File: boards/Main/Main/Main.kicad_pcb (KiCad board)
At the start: 2 copper layers, 32 parts, among them J1 CAN_H, J10 Status_Light, J11 J00-0045NL, J12 IMU, J2 GND, J3 TX/RX, J4 5V, J5 Digital I/O, J6 CAN_Board, J7 CAN_L, J8 CAN H/L, J9 24V, K1 G5LE-1, K2 G5LE-1, K3 G5LE-1, K4 G5LE-1, Q1 2N3904, Q2 2N3904, Q3 2N3904, U1 Teensy4.1, U2 BNO055

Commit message: Updated Main PCB
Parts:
- removed 0.1uF1: C, Capacitor_THT:CP_Axial_L10.0mm_D4.5mm_P15.00mm_Horizontal
- removed CB1: Break1, Connector_PinHeader_2.54mm:PinHeader_1x01_P2.54mm_Vertical
- removed CB2: Break2, Connector_PinHeader_2.54mm:PinHeader_1x02_P2.54mm_Horizontal
- removed J1: CAN_H, Connector_PinHeader_2.54mm:PinHeader_1x01_P2.54mm_Vertical
- removed J10: Status_Light, Connector_PinHeader_2.54mm:PinHeader_1x04_P2.54mm_Vertical
- removed J11: J00-0045NL, teensy.pretty-master:PULSE_J00-0045NL
- removed J12: IMU, Connector_PinHeader_2.54mm:PinHeader_1x03_P2.54mm_Vertical
- removed J2: GND, Connector_PinHeader_2.54mm:PinHeader_1x04_P2.54mm_Vertical
- removed J3: TX/RX, Connector_PinHeader_2.54mm:PinHeader_1x02_P2.54mm_Vertical
- removed J4: 5V, Connector_PinHeader_2.54mm:PinHeader_1x04_P2.54mm_Vertical
- removed J5: Digital I/O, Connector_PinHeader_2.54mm:PinHeader_1x04_P2.54mm_Vertical
- removed J6: CAN_Board, Connector_PinHeader_2.54mm:PinHeader_1x04_P2.54mm_Vertical
- removed J7: CAN_L, Connector_PinHeader_2.54mm:PinHeader_1x01_P2.54mm_Vertical
- removed J8: CAN H/L, Connector_PinHeader_2.54mm:PinHeader_1x01_P2.54mm_Vertical
- removed J9: 24V, Connector_PinHeader_2.54mm:PinHeader_1x02_P2.54mm_Vertical
- removed K1, K2, K3, K4: G5LE-1, Relay_THT:Relay_SPDT_Omron-G5LE-1
- removed U1: Teensy4.1, teensy.pretty-master:Teensy41
- removed U2: BNO055, Package_LGA:LGA-28_5.2x3.8mm_P0.5mm
- added 24V_Pin1: 24V, Connector_PinHeader_2.54mm:PinHeader_1x02_P2.54mm_Vertical, F.Cu at (96.8, 88.7)
- added 5V_Pin1: 5V, Connector_PinHeader_2.54mm:PinHeader_1x02_P2.54mm_Vertical, F.Cu at (96.8, 92.4)
- added C1: 0.1uF, Capacitor_THT:CP_Axial_L10.0mm_D4.5mm_P15.00mm_Horizontal, F.Cu at (122.7, 66.2)
- added CAN_Board1: CAN_Board, Connector_PinHeader_2.54mm:PinHeader_1x04_P2.54mm_Vertical, F.Cu at (129.5, 56.5)
- added CAN_H1: CAN_H, Connector_PinHeader_2.54mm:PinHeader_1x01_P2.54mm_Vertical, F.Cu at (134.0, 68.0)
- added CAN_L1: CAN_L, Connector_PinHeader_2.54mm:PinHeader_1x01_P2.54mm_Vertical, F.Cu at (134.0, 53.2)
- added CAN_OUT1: CAN_pins, Connector_PinHeader_2.54mm:PinHeader_2x09_P2.54mm_Vertical, F.Cu at (159.0, 50.4)
- added Digital_I/O1: Digital I/O, Connector_PinHeader_2.54mm:PinHeader_1x04_P2.54mm_Vertical, F.Cu at (96.8, 109.9)
- added Ethernet1: J00-0045NL, teensy.pretty-master:PULSE_J00-0045NL, F.Cu at (103.6, 58.6)
- added Ethernet_Cable1: Conn_02x03_Odd_Even, Connector_PinHeader_2.54mm:PinHeader_2x03_P2.54mm_Vertical, F.Cu at (114.7, 56.5)
- added GND_Pin1: GND, Connector_PinHeader_2.54mm:PinHeader_1x04_P2.54mm_Vertical, F.Cu at (96.8, 98.6)
- added IMU1: IMU, Connector_PinHeader_2.54mm:PinHeader_1x03_P2.54mm_Vertical, F.Cu at (96.8, 126.5)
- added RTX_Pin1: TX/RX, Connector_PinHeader_2.54mm:PinHeader_1x02_P2.54mm_Vertical, F.Cu at (96.8, 79.9)
- added Relay_1: G5LE1_Green, Relay_THT:Relay_SPDT_Omron-G5LE-1, F.Cu at (154.5, 129.9)
- added Relay_2: G5LE1_Blue, Relay_THT:Relay_SPDT_Omron-G5LE-1, F.Cu at (154.5, 87.8)
- added Relay_3: G5LE1_Red, Relay_THT:Relay_SPDT_Omron-G5LE-1, F.Cu at (136.8, 88.0)
- added Status_Light1: Status_Light, Connector_PinHeader_2.54mm:PinHeader_1x04_P2.54mm_Vertical, F.Cu at (145.2, 82.0)
- added Teensy4.1: Teensy4.1, teensy.pretty-master:Teensy41, F.Cu at (109.4, 103.6)
- D1, D2, D3: footprint LED_THT:LED_D5.0mm-3 -> LED_THT:LED_D5.0mm
- moved D1 80.8 mm to (139.8, 127.2), turned to -90 degrees
- moved D2 72.0 mm to (140.0, 118.4), turned to -90 degrees
- moved R1 69.7 mm to (122.5, 130.4), turned to 90 degrees
- moved D3 66.8 mm to (140.0, 111.7), turned to -90 degrees
- moved R2 47.2 mm to (122.5, 110.4), turned to 90 degrees
- moved Q1 45.8 mm to (131.8, 128.8), turned to -90 degrees
- moved Q2 34.7 mm to (131.8, 120.5), turned to -90 degrees
- moved R5 31.8 mm to (139.5, 52.8), turned to -90 degrees
- moved R3 29.9 mm to (122.5, 92.4), turned to 90 degrees
- moved Q3 27.1 mm to (131.8, 113.8), turned to -90 degrees
- moved R4 12.2 mm to (151.8, 68.1), turned to 90 degrees
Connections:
- Q1 pad 3: Net-(D2-A) -> Net-(D1-A)
- Q2 pad 3: Net-(D1-A) -> Net-(D2-A)
- R1 pad 2: Net-(Q2-B) -> Net-(Q1-B)
- R2 pad 2: Net-(Q1-B) -> Net-(Q2-B)
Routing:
- net +5V: track 0.00 -> 214.8 mm
- net GND: track 0.00 -> 197.4 mm
- net +24V: track 0.00 -> 97.2 mm
- net /M1H: track 0.00 -> 78.2 mm
- net Net-(Q2-B): track 0.00 -> 60.2 mm
- net /M1L: track 0.00 -> 51.6 mm
- net Net-(D2-A): track 0.00 -> 48.7 mm
- net Net-(D1-A): track 0.00 -> 46.6 mm
- net Net-(Teensy4.1-30_CRX3): track 0.00 -> 43.9 mm
- net Net-(Q3-B): track 0.00 -> 43.6 mm
- net /Status_G: track 0.00 -> 41.6 mm, vias 0 -> 1
- net Net-(D3-A): track 0.00 -> 39.8 mm
- net Net-(Ethernet1-GND): track 0.00 -> 39.1 mm
- net /Status_R: track 0.00 -> 34.3 mm, vias 0 -> 2
- net Net-(Teensy4.1-31_CTX3): track 0.00 -> 33.5 mm
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- added copper zone on B.Cu, net GND
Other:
- board outline added: 76 x 92.5 mm
- board text added: "24V"
- board text added: "3.3V"
- board text added: "3V3"
- board text added: "5V"
- board text added: "B"
- board text added: "CAN Board"
- board text added: "CAN H/L"
- board text added: "CAN_H"
- board text added: "CAN_L"
- board text added: "CRX"
- board text added: "CTX"
- board text added: "Cable"
- board text added: "D1"
- board text added: "D2"
- board text added: "D3"
- board text added: "D4"
- board text added: "DRAIN"
- board text added: "Ethernet"
- board text added: "G"
- board text added: "GATE"
- board text added: "GND"
- board text added: "HIGH"
- board text added: "LOW"
- board text added: "R"
- board text added: "R-"
- board text added: "RX"
- board text added: "SCL"
- board text added: "SDA"
- board text added: "TX"

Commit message: Add files via upload
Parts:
- moved Ethernet_Cable1 29.3 mm to (135.7, 77.0)
- moved Ethernet1 23.3 mm to (126.8, 60.0)
- moved C1 16.3 mm to (139.0, 67.5)
- moved CAN_Board1 15.8 mm to (145.2, 56.7)
- moved CAN_H1 11.3 mm to (145.2, 68.2)
- moved CAN_L1 11.3 mm to (145.2, 53.0)
- moved R5 9.50 mm to (149.0, 52.9)
- moved R4 1.50 mm to (153.2, 68.1)
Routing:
- net +24V: track 97.2 -> 181.8 mm
- net Net-(Ethernet1-RD-): track 19.3 -> 78.8 mm, vias 1 -> 0
- net Net-(Ethernet1-LA): track 13.0 -> 51.1 mm
- net Net-(Ethernet1-GND): track 39.1 -> 64.9 mm
- net GND: track 197.4 -> 213.1 mm
- net /M1H: track 78.2 -> 63.5 mm
- net Net-(Ethernet1-CTR): track 23.0 -> 37.6 mm
- net /M1L: track 51.6 -> 37.5 mm
- net Net-(CAN_Board1-Pin_2): track 25.2 -> 37.9 mm
- net Net-(CAN_Board1-Pin_3): track 26.2 -> 37.0 mm
- net Net-(CAN_Board1-Pin_4): track 27.5 -> 36.6 mm
- net Net-(Ethernet1-TD-): track 13.0 -> 20.0 mm
- net Net-(Ethernet1-RD+): track 18.0 -> 15.1 mm
- net Net-(Ethernet1-TD+): track 18.9 -> 17.5 mm
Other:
- board size 76 x 92.5 mm -> 74.8 x 91 mm
- board text removed: "CAN Board"

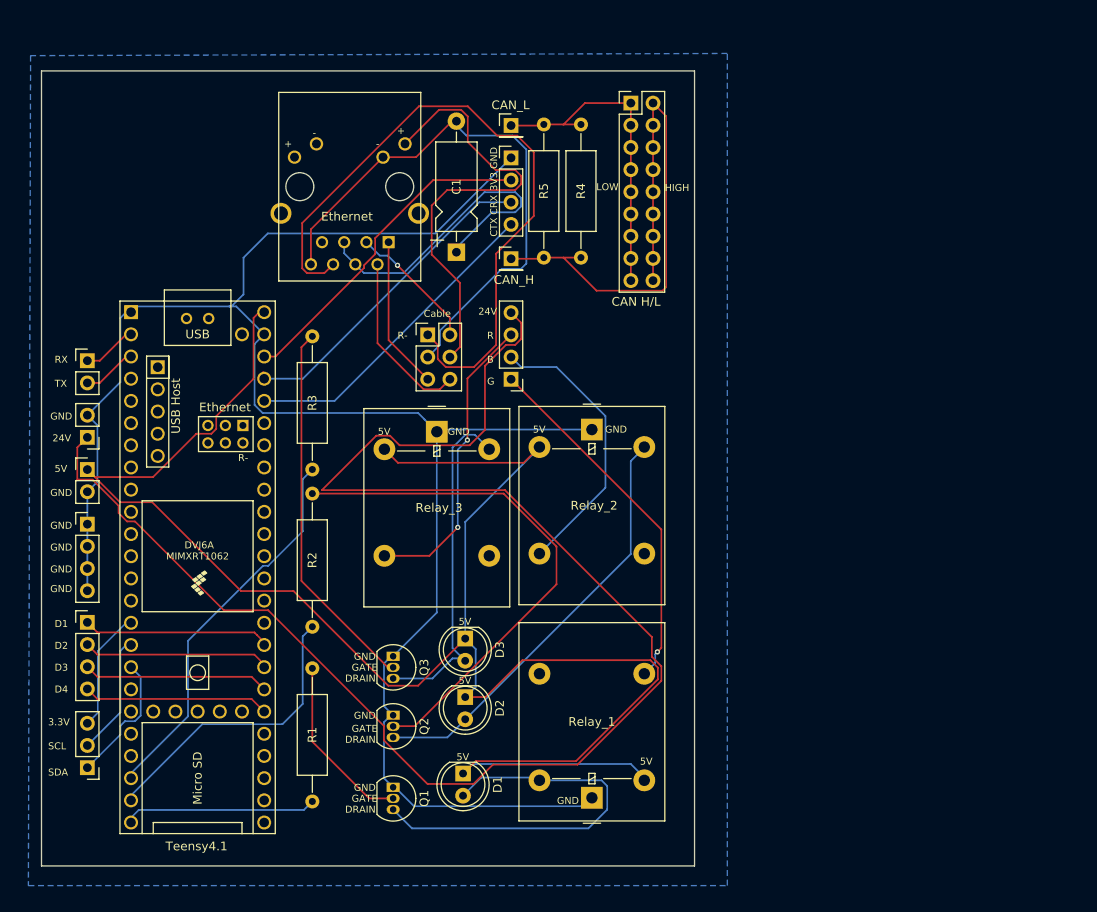
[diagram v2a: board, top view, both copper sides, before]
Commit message: Switched RX/TX pin position and IMU pin position
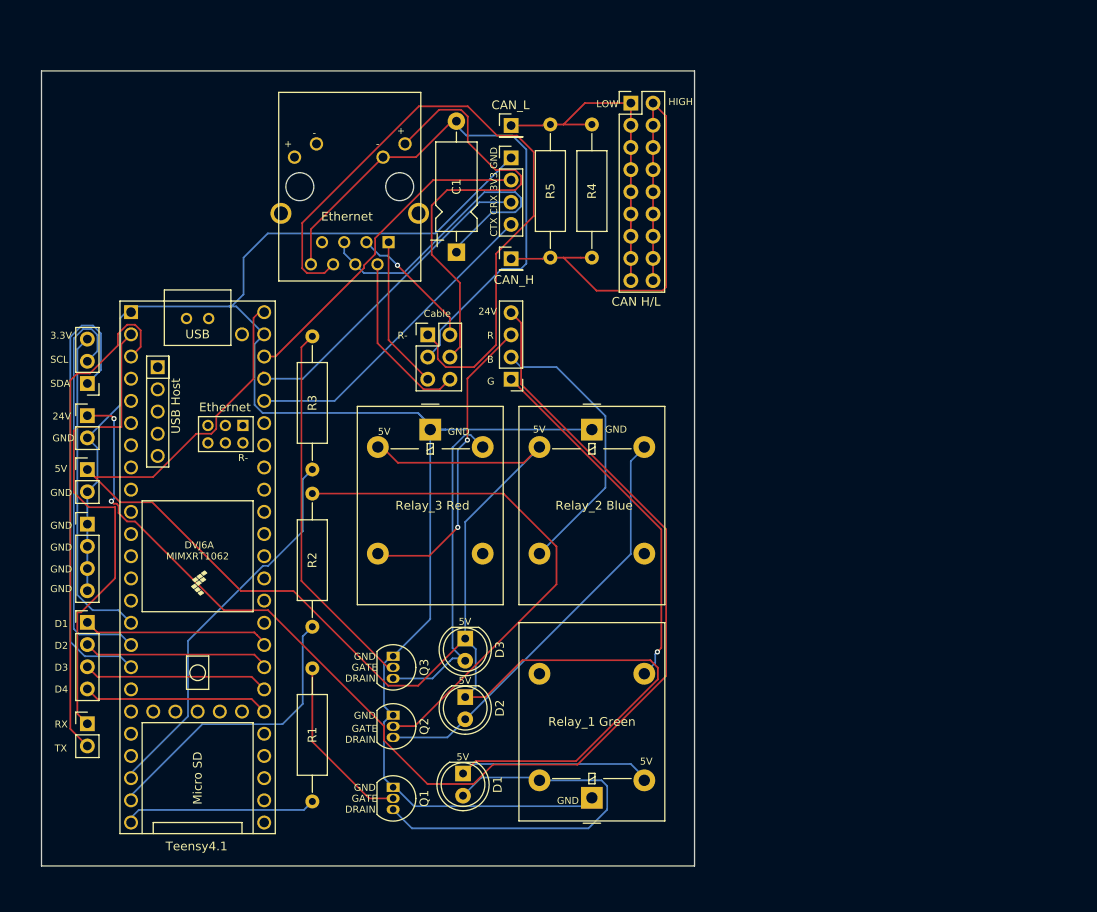
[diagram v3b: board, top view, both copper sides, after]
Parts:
- Relay_1 Green: renamed from Relay_1
- Relay_2 Blue: renamed from Relay_2
- Relay_3 Red: renamed from Relay_3
- moved IMU1 44.0 mm to (96.8, 82.5)
- moved RTX_Pin1 41.6 mm to (96.8, 121.5)
- moved 24V_Pin1 2.48 mm to (96.8, 86.2), turned to 0 degrees
- moved R4 1.25 mm to (154.5, 68.1)
- moved Relay_3 Red 0.79 mm to (136.0, 87.8)
- moved R5 0.75 mm to (149.8, 52.9)
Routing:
- net /TX1: track 6.31 -> 57.8 mm
- net /RX1: track 6.31 -> 56.5 mm
- net /SDA2: track 15.2 -> 53.8 mm
- net +24V: track 181.8 -> 145.2 mm, vias 0 -> 2
- net /SCL2: track 14.0 -> 47.5 mm
- net /3.3V: track 14.0 -> 37.2 mm
- net GND: track 213.1 -> 217.2 mm
- net /M1H: track 63.5 -> 64.8 mm
- net /M1L: track 37.5 -> 38.7 mm
- net Net-(D3-A): track 39.8 -> 39.0 mm
- net /Status_R: track 34.3 -> 35.2 mm
- net +5V: track 214.8 -> 215.7 mm
- removed copper zone on B.Cu, net GND

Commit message: Added Logo
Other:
- board text added: "Micro SD"
- board text added: "URC Main Electrical Board v1.0"
- board text removed: "DRAIN"
- board text removed: "GATE"

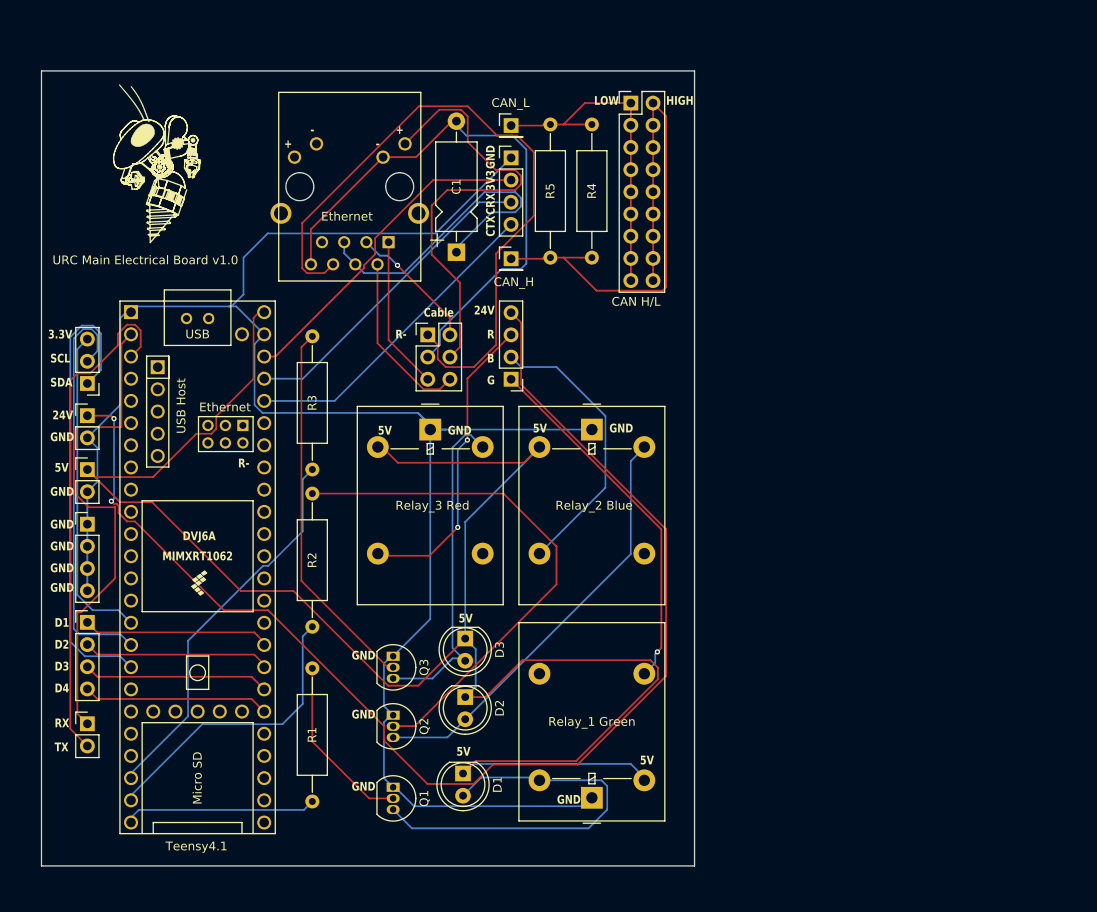
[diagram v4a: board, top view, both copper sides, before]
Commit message: Added Holes to Main PCB
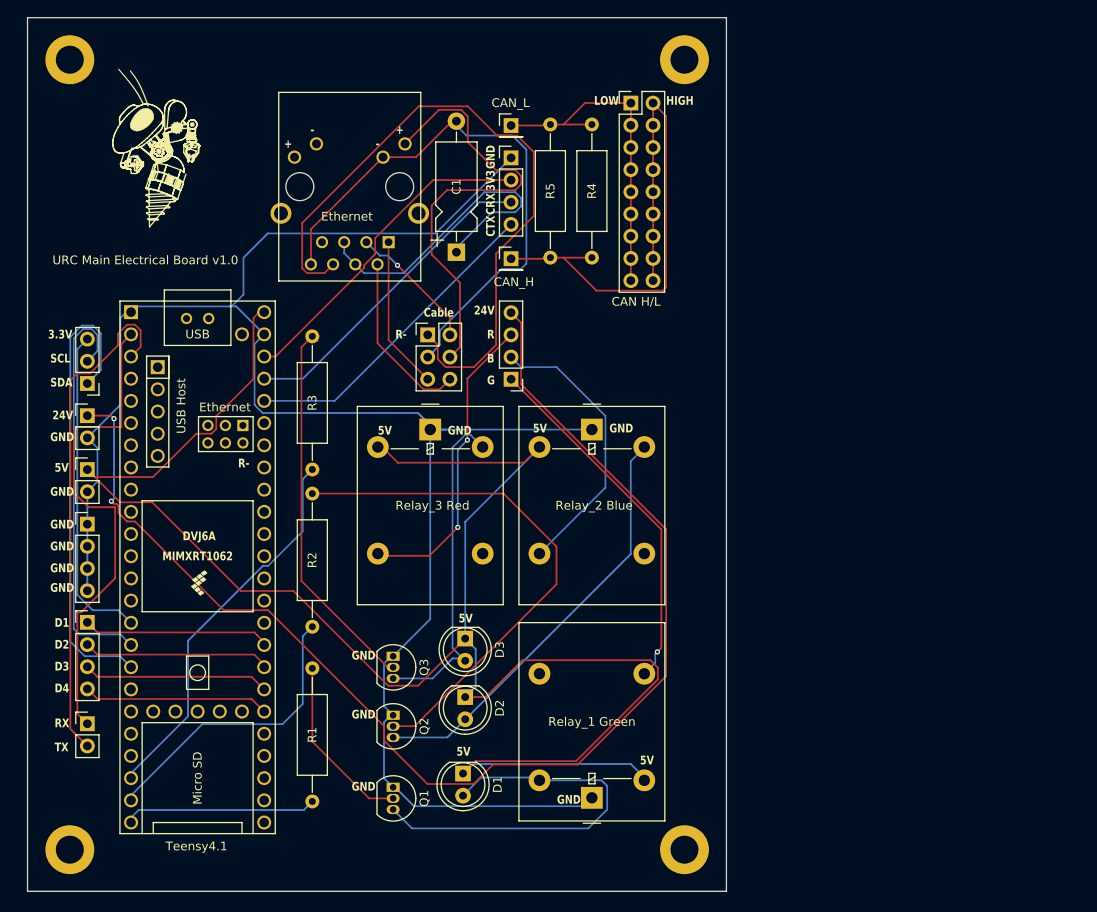
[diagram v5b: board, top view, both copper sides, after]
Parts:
- added GND: MountingHole_3.2mm_M3_DIN965_Pad, MountingHole:MountingHole_3.2mm_M3_DIN965_Pad, F.Cu at (94.7, 135.9)
- added REF**: MountingHole_3.2mm_M3_DIN965_Pad, MountingHole:MountingHole_3.2mm_M3_DIN965_Pad, F.Cu at (165.1, 45.5)
- added REF**: MountingHole_3.2mm_M3_DIN965_Pad, MountingHole:MountingHole_3.2mm_M3_DIN965_Pad, F.Cu at (165.1, 135.9)
- added REF**: MountingHole_3.2mm_M3_DIN965_Pad, MountingHole:MountingHole_3.2mm_M3_DIN965_Pad, F.Cu at (94.7, 45.5)
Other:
- board size 74.8 x 91 mm -> 80 x 100 mm
- board text added: "Protoboard Dimensions: 88.8mm X 127mm New Dimensions: 100mm x 80mm"

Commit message: updated main board
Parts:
- Relay_1: renamed from Relay_1 Green
- Relay_2: renamed from Relay_2 Blue
- Relay_3: renamed from Relay_3 Red
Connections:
- CAN_Board1 pad 2: Net-(CAN_Board1-Pin_2) -> /3.3V
- Teensy4.1 pad 15: /3.3V -> unconnected-(Teensy4.1-3V3-Pad15)
- Teensy4.1 pad 46: Net-(CAN_Board1-Pin_2) -> /3.3V
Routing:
- net Net-(CAN_Board1-Pin_2): track 37.9 -> 0.00 mm
- net /3.3V: track 37.2 -> 68.1 mm
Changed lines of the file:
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@@
 	(net 14 "Net-(CAN_Board1-Pin_3)")
 	(net 15 "Net-(CAN_Board1-Pin_4)")
-	(net 16 "Net-(CAN_Board1-Pin_2)")
+	(net 16 "unconnected-(Teensy4.1-3V3-Pad15)")
 	(net 17 "unconnected-(Ethernet1-RA-Pad12)")
 	(net 18 "/RX1")
@@
 			(layers "*.Cu" "*.Mask")
 			(remove_unused_layers no)
-			(net 16 "Net-(CAN_Board1-Pin_2)")
+			(net 19 "/3.3V")
 			(pinfunction "Pin_2")
 			(pintype "passive")
@@
 		(descr "Omron Relay SPDT, http://www.omron.com/ecb/products/pdf/en-g5le.pdf")
 		(tags "Omron Relay SPDT")
-		(property "Reference" "Relay_1 Green"
+		(property "Reference" "Relay_1"
 			(at 0 8.7 180)
 			(layer "F.SilkS")
@@
 		(descr "Omron Relay SPDT, http://www.omron.com/ecb/products/pdf/en-g5le.pdf")
 		(tags "Omron Relay SPDT")
-		(property "Reference" "Relay_2 Blue"
+		(property "Reference" "Relay_2"
 			(at 0.25 8.7 0)
 			(layer "F.SilkS")
@@
 			(layers "*.Cu" "*.Mask")
 			(remove_unused_layers no)
-			(net 19 "/3.3V")
+			(net 16 "unconnected-(Teensy4.1-3V3-Pad15)")
 			(pinfunction "3V3")
-			(pintype "power_out")
+			(pintype "power_out+no_connect")
 		)
 		(pad "16" thru_hole circle
@@
 			(layers "*.Cu" "*.Mask")
 			(remove_unused_layers no)
-			(net 16 "Net-(CAN_Board1-Pin_2)")
+			(net 19 "/3.3V")
 			(pinfunction "3V3")
 			(pintype "output")
@@
 		(descr "Omron Relay SPDT, http://www.omron.com/ecb/products/pdf/en-g5le.pdf")
 		(tags "Omron Relay SPDT")
-		(property "Reference" "Relay_3 Red"
+		(property "Reference" "Relay_3"
 			(at 0.25 8.7 0)
 			(layer "F.SilkS")
@@
 	)
 	(segment
-		(start 118.2828 79.44)
-		(end 116.99 79.44)
-		(width 0.2)
-		(layer "F.Cu")
-		(net 16)
-	)
-	(segment
-		(start 128.419 69)
-		(end 128.419 69.3038)
-		(width 0.2)
-		(layer "F.Cu")
-		(net 16)
-	)
-	(segment
-		(start 145.25 59.24)
-		(end 136.342 59.24)
-		(width 0.2)
-		(layer "F.Cu")
-		(net 16)
-	)
-	(segment
-		(start 136.342 59.24)
-		(end 129.689 65.893)
-		(width 0.2)
-		(layer "F.Cu")
-		(net 16)
-	)
-	(segment
-		(start 129.689 67.73)
-		(end 128.419 69)
-		(width 0.2)
-		(layer "F.Cu")
-		(net 16)
-	)
-	(segment
-		(start 129.689 65.893)
-		(end 129.689 67.73)
-		(width 0.2)
-		(layer "F.Cu")
-		(net 16)
-	)
-	(segment
-		(start 128.419 69.3038)
-		(end 118.2828 79.44)
-		(width 0.2)
-		(layer "F.Cu")
-		(net 16)
-	)
-	(segment
 		(start 100.65 78)
 		(end 101.75 76.9)
@@
 	)
 	(segment
-		(start 97.353654 108.48)
-		(end 100.31 108.48)
+		(start 117.76 73.26)
+		(end 118.09 73.59)
 		(width 0.2)
-		(layer "B.Cu")
+		(layer "F.Cu")
+		(net 19)
+	)
+	(segment
+		(start 118.09 73.59)
+		(end 118.09 78.34)
+		(width 0.2)
+		(layer "F.Cu")
 		(net 19)
 	)
 	(segment
 		(start 96.75 77.445)
-		(end 95.6 78.595)
+		(end 96.75 76.242919)
 		(width 0.2)
-		(layer "B.Cu")
+		(layer "F.Cu")
 		(net 19)
 	)
 	(segment
-		(start 100.31 108.48)
-		(end 101.75 109.92)
+		(start 118.09 78.34)
+		(end 116.99 79.44)
 		(width 0.2)
-		(layer "B.Cu")
+		(layer "F.Cu")
 		(net 19)
 	)
 	(segment
-		(start 95.6 106.726346)
-		(end 97.353654 108.48)
+		(start 96.75 76.242919)
+		(end 99.732919 73.26)
 		(width 0.2)
-		(layer "B.Cu")
+		(layer "F.Cu")
 		(net 19)
 	)
 	(segment
-		(start 95.6 78.595)
-		(end 95.6 106.726346)
+		(start 118.2828 79.44)
+		(end 116.99 79.44)
 		(width 0.2)
-		(layer "B.Cu")
+		(layer "F.Cu")
+		(net 19)
+	)
+	(segment
+		(start 128.419 69)
+		(end 128.419 69.3038)
+		(width 0.2)
+		(layer "F.Cu")
+		(net 19)
+	)
+	(segment
+		(start 145.25 59.24)
+		(end 136.342 59.24)
+		(width 0.2)
+		(layer "F.Cu")
+		(net 19)
+	)
+	(segment
+		(start 136.342 59.24)
+		(end 129.689 65.893)
+		(width 0.2)
+		(layer "F.Cu")
+		(net 19)
+	)
+	(segment
+		(start 129.689 67.73)
+		(end 128.419 69)
+		(width 0.2)
+		(layer "F.Cu")
+		(net 19)
+	)
+	(segment
+		(start 129.689 65.893)
+		(end 129.689 67.73)
+		(width 0.2)
+		(layer "F.Cu")
+		(net 19)
+	)
+	(segment
+		(start 128.419 69.3038)
+		(end 118.2828 79.44)
+		(width 0.2)
+		(layer "F.Cu")
+		(net 19)
+	)
+	(segment
+		(start 99.732919 73.26)
+		(end 117.76 73.26)
+		(width 0.2)
+		(layer "F.Cu")
 		(net 19)
 	)
